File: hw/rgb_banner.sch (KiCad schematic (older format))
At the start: 8 parts, among them P1 TST, P2 TST, P3 TST, P4 TST, U1 WS2812B, U2 WS2812B, U3 WS2812B, U4 WS2812B

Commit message: schematic pretty much done, start layout
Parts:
- removed U1, U2, U3, U4: WS2812B, symbol WS2812B
- added P4: +5V, kicadlib:TEST_0.100, symbol TST
- added P5: GND, kicadlib:TEST_0.100, symbol TST
- P1: value TST -> +5V; footprint (none) -> kicadlib:TEST_0.100
- P2: value TST -> GND; footprint (none) -> kicadlib:TEST_0.100
- P3: value TST -> DIN; footprint (none) -> kicadlib:TEST_0.100
- P6: renamed from P4; value TST -> DOUT; footprint (none) -> kicadlib:TEST_0.100
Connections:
- net labels added: gnd
- net labels removed: GND
- wire segments 27 -> 19
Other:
- moved on the sheet: P1, P2, P3, P6
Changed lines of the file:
@@
 $Descr A4 11693 8268
 encoding utf-8
-Sheet 1 1
+Sheet 1 3
 Title ""
 Date ""
@@
 $EndDescr
 $Comp
-L WS2812B U1
-U 1 1 556C6577
-P 4050 2100
-F 0 "U1" H 4050 1850 60  0000 C CNN
-F 1 "WS2812B" H 4050 2300 60  0000 C CNN
-F 2 "" H 4350 1950 60  0000 C CNN
-F 3 "" H 4350 1950 60  0000 C CNN
-	1    4050 2100
-	-1   0    0    1
-$EndComp
-$Comp
-L WS2812B U2
-U 1 1 556C661E
-P 5150 2100
-F 0 "U2" H 5150 1850 60  0000 C CNN
-F 1 "WS2812B" H 5150 2300 60  0000 C CNN
-F 2 "" H 5450 1950 60  0000 C CNN
-F 3 "" H 5450 1950 60  0000 C CNN
-	1    5150 2100
-	-1   0    0    1
-$EndComp
-$Comp
-L WS2812B U3
-U 1 1 556C6646
-P 6250 2100
-F 0 "U3" H 6250 1850 60  0000 C CNN
-F 1 "WS2812B" H 6250 2300 60  0000 C CNN
-F 2 "" H 6550 1950 60  0000 C CNN
-F 3 "" H 6550 1950 60  0000 C CNN
-	1    6250 2100
-	-1   0    0    1
-$EndComp
-$Comp
-L WS2812B U4
-U 1 1 556C6673
-P 7350 2100
-F 0 "U4" H 7350 1850 60  0000 C CNN
-F 1 "WS2812B" H 7350 2300 60  0000 C CNN
-F 2 "" H 7650 1950 60  0000 C CNN
-F 3 "" H 7650 1950 60  0000 C CNN
-	1    7350 2100
-	-1   0    0    1
-$EndComp
-Text Label 3350 2500 2    60   ~ 0
-+5V
-$Comp
-L GND #PWR01
-U 1 1 556C66A2
-P 3350 1800
-F 0 "#PWR01" H 3350 1800 30  0001 C CNN
-F 1 "GND" H 3350 1730 30  0001 C CNN
-F 2 "" H 3350 1800 60  0000 C CNN
-F 3 "" H 3350 1800 60  0000 C CNN
-	1    3350 1800
-	1    0    0    -1
-$EndComp
-Wire Wire Line
-	3600 2000 3600 1700
-Wire Wire Line
-	3350 1700 5800 1700
-Wire Wire Line
-	3350 1700 3350 1800
-Text Label 3350 2150 2    60   ~ 0
-d_in
-Wire Wire Line
-	3350 2150 3600 2150
-Wire Wire Line
-	3350 2500 7800 2500
-Wire Wire Line
-	4500 2500 4500 2150
-Wire Wire Line
-	4500 2000 4600 2000
-Wire Wire Line
-	4600 2000 4600 2150
-Wire Wire Line
-	4600 2150 4700 2150
-Wire Wire Line
-	5600 2000 5700 2000
-Wire Wire Line
-	5700 2000 5700 2150
-Wire Wire Line
-	5700 2150 5800 2150
-Wire Wire Line
-	5600 2500 5600 2150
-Connection ~ 4500 2500
-Wire Wire Line
-	4700 1700 4700 2000
-Connection ~ 3600 1700
-Wire Wire Line
-	5800 1700 5800 2000
-Connection ~ 4700 1700
-Wire Wire Line
-	5850 1700 6900 1700
-Wire Wire Line
-	6900 1700 6900 2000
-Wire Wire Line
-	6700 2500 6700 2150
-Connection ~ 5600 2500
-Wire Wire Line
-	7800 2500 7800 2150
-Connection ~ 6700 2500
-Wire Wire Line
-	6700 2000 6800 2000
-Wire Wire Line
-	6800 2000 6800 2150
-Wire Wire Line
-	6800 2150 6900 2150
-Text Label 7900 2000 0    60   ~ 0
-d_out
-Wire Wire Line
-	7900 2000 7800 2000
-$Comp
 L TST P1
 U 1 1 556C686B
-P 1850 2100
-F 0 "P1" H 1850 2400 40  0000 C CNN
-F 1 "TST" H 1850 2350 30  0000 C CNN
-F 2 "" H 1850 2100 60  0000 C CNN
-F 3 "" H 1850 2100 60  0000 C CNN
-	1    1850 2100
+P 4350 3500
+F 0 "P1" H 4350 3800 40  0000 C CNN
+F 1 "+5V" H 4350 3750 30  0000 C CNN
+F 2 "kicadlib:TEST_0.100" H 4350 3500 60  0001 C CNN
+F 3 "" H 4350 3500 60  0000 C CNN
+	1    4350 3500
 	1    0    0    -1
 $EndComp
@@
 L TST P2
 U 1 1 556C69BB
-P 2000 2200
-F 0 "P2" H 2000 2500 40  0000 C CNN
-F 1 "TST" H 2000 2450 30  0000 C CNN
-F 2 "" H 2000 2200 60  0000 C CNN
-F 3 "" H 2000 2200 60  0000 C CNN
-	1    2000 2200
+P 4050 3650
+F 0 "P2" H 4050 3950 40  0000 C CNN
+F 1 "GND" H 4050 3900 30  0000 C CNN
+F 2 "kicadlib:TEST_0.100" H 4050 3650 60  0001 C CNN
+F 3 "" H 4050 3650 60  0000 C CNN
+	1    4050 3650
 	1    0    0    -1
 $EndComp
@@
 L TST P3
 U 1 1 556C69DB
-P 2150 2300
-F 0 "P3" H 2150 2600 40  0000 C CNN
-F 1 "TST" H 2150 2550 30  0000 C CNN
-F 2 "" H 2150 2300 60  0000 C CNN
-F 3 "" H 2150 2300 60  0000 C CNN
-	1    2150 2300
+P 3750 3800
+F 0 "P3" H 3750 4100 40  0000 C CNN
+F 1 "DIN" H 3750 4050 30  0000 C CNN
+F 2 "kicadlib:TEST_0.100" H 3750 3800 60  0001 C CNN
+F 3 "" H 3750 3800 60  0000 C CNN
+	1    3750 3800
 	1    0    0    -1
 $EndComp
 $Comp
-L TST P4
+L TST P6
 U 1 1 556C69FA
-P 2300 2400
-F 0 "P4" H 2300 2700 40  0000 C CNN
-F 1 "TST" H 2300 2650 30  0000 C CNN
-F 2 "" H 2300 2400 60  0000 C CNN
-F 3 "" H 2300 2400 60  0000 C CNN
-	1    2300 2400
+P 7050 3800
+F 0 "P6" H 7050 4100 40  0000 C CNN
+F 1 "DOUT" H 7050 4050 30  0000 C CNN
+F 2 "kicadlib:TEST_0.100" H 7050 3800 60  0001 C CNN
+F 3 "" H 7050 3800 60  0000 C CNN
+	1    7050 3800
 	1    0    0    -1
 $EndComp
-Text Label 1850 2200 3    60   ~ 0
+Text Label 4300 3600 2    60   ~ 0
 +5V
+Text Label 3700 3900 2    60   ~ 0
+d_in
+Text Label 7100 3900 0    60   ~ 0
+d_out
+Wire Wire Line
+	3750 3800 3750 3900
+Wire Wire Line
+	4050 3750 4050 3650
+Wire Wire Line
+	4350 3600 4350 3500
 $Comp
-L GND #PWR02
-U 1 1 556C6A24
-P 2000 2300
-F 0 "#PWR02" H 2000 2300 30  0001 C CNN
-F 1 "GND" H 2000 2230 30  0001 C CNN
-F 2 "" H 2000 2300 60  0000 C CNN
-F 3 "" H 2000 2300 60  0000 C CNN
-	1    2000 2300
+L TST P4
+U 1 1 556C71D9
+P 6450 3500
+F 0 "P4" H 6450 3800 40  0000 C CNN
+F 1 "+5V" H 6450 3750 30  0000 C CNN
+F 2 "kicadlib:TEST_0.100" H 6450 3500 60  0001 C CNN
+F 3 "" H 6450 3500 60  0000 C CNN
+	1    6450 3500
 	1    0    0    -1
 $EndComp
-Text Label 2150 2400 3    60   ~ 0
-d_in
-Text Label 2300 2500 3    60   ~ 0
-d_out
+$Comp
+L TST P5
+U 1 1 556C71DF
+P 6750 3650
+F 0 "P5" H 6750 3950 40  0000 C CNN
+F 1 "GND" H 6750 3900 30  0000 C CNN
+F 2 "kicadlib:TEST_0.100" H 6750 3650 60  0001 C CNN
+F 3 "" H 6750 3650 60  0000 C CNN
+	1    6750 3650
+	1    0    0    -1
+$EndComp
+Text Label 6500 3600 0    60   ~ 0
++5V
 Wire Wire Line
-	2300 2500 2300 2400
+	6450 3600 6450 3500
+Text Label 4000 3750 2    60   ~ 0
+gnd
+$Sheet
+S 5600 3500 750  1600
+U 556C8A1A
+F0 "digit2" 60
+F1 "digit2.sch" 60
+F2 "gnd" I R 6350 3750 60
+F3 "+5V" I R 6350 3600 60
+F4 "d_in_1" I L 5600 4050 60
+F5 "d_out_all" I R 6350 3900 60
+F6 "d_in_2" I L 5600 4350 60
+F7 "d_in_3" I L 5600 4650 60
+F8 "d_out_1" I L 5600 4200 60
+F9 "d_out_2" I L 5600 4500 60
+F10 "d_out_3" I L 5600 4800 60
+F11 "d_in_4" I L 5600 4950 60
+$EndSheet
 Wire Wire Line
-	2150 2300 2150 2400
+	3700 3900 4450 3900
 Wire Wire Line
-	2000 2300 2000 2200
+	4000 3750 4450 3750
 Wire Wire Line
-	1850 2200 1850 2100
+	4300 3600 4450 3600
+Connection ~ 4350 3600
+Connection ~ 4050 3750
+Connection ~ 3750 3900
+Text Label 6800 3750 0    60   ~ 0
+gnd
+Wire Wire Line
+	6350 3600 6500 3600
+Connection ~ 6450 3600
+Wire Wire Line
+	6350 3750 6800 3750
+Wire Wire Line
+	6750 3750 6750 3650
+Wire Wire Line
+	6350 3900 7100 3900
+Wire Wire Line
+	7050 3900 7050 3800
+Connection ~ 6750 3750
+Connection ~ 7050 3900
+$Sheet
+S 4450 3500 750  1600
+U 556C8146
+F0 "digit1" 60
+F1 "digit1.sch" 60
+F2 "gnd" I L 4450 3750 60
+F3 "+5V" I L 4450 3600 60
+F4 "d_in_all" I L 4450 3900 60
+F5 "d_out_3" I R 5200 4650 60
+F6 "d_out_4" I R 5200 4950 60
+F7 "d_in_3" I R 5200 4800 60
+F8 "d_in_2" I R 5200 4500 60
+F9 "d_out_2" I R 5200 4350 60
+F10 "d_in_1" I R 5200 4200 60
+F11 "d_out_1" I R 5200 4050 60
+$EndSheet
+Wire Wire Line
+	5200 4050 5600 4050
+Wire Wire Line
+	5600 4200 5200 4200
+Wire Wire Line
+	5200 4350 5600 4350
+Wire Wire Line
+	5600 4500 5200 4500
+Wire Wire Line
+	5200 4650 5600 4650
+Wire Wire Line
+	5600 4800 5200 4800
+Wire Wire Line
+	5200 4950 5600 4950
 $EndSCHEMATC

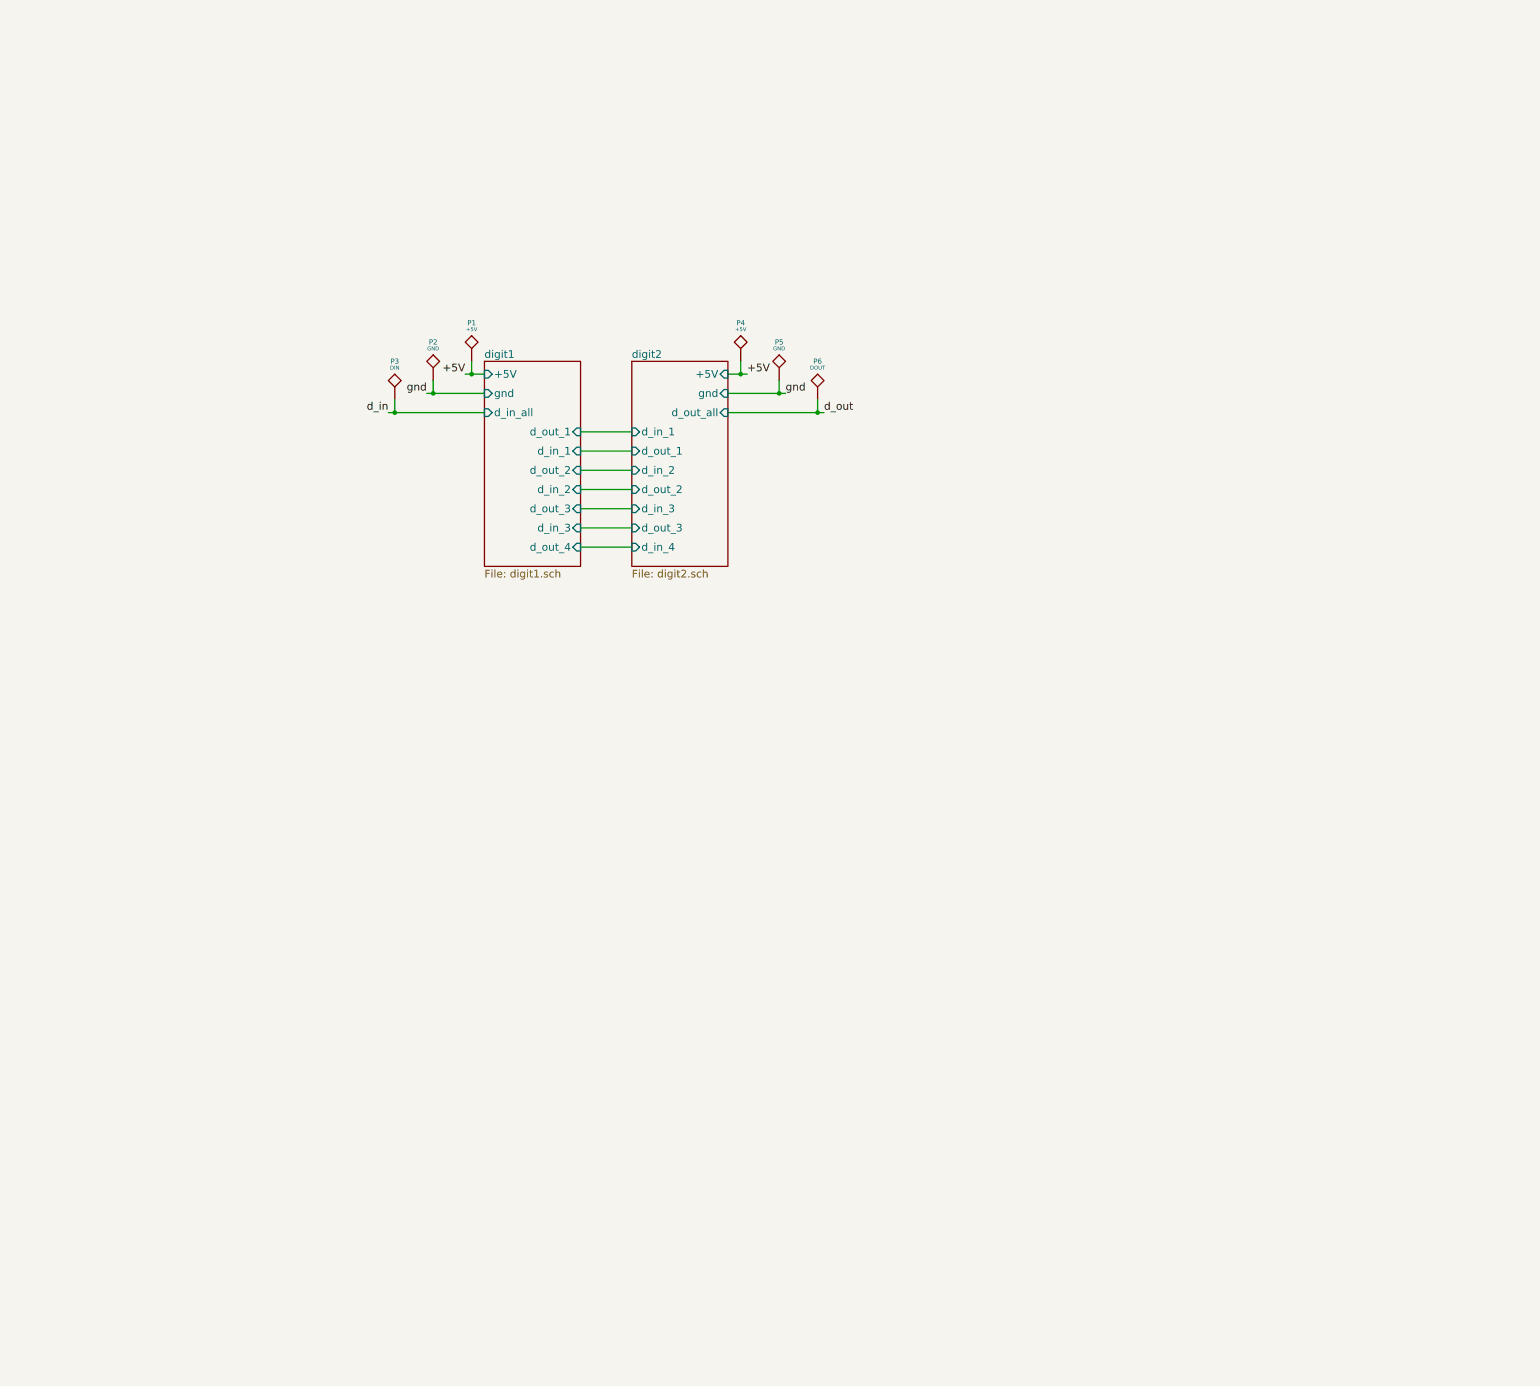
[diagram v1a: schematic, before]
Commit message: start consolidating schematic
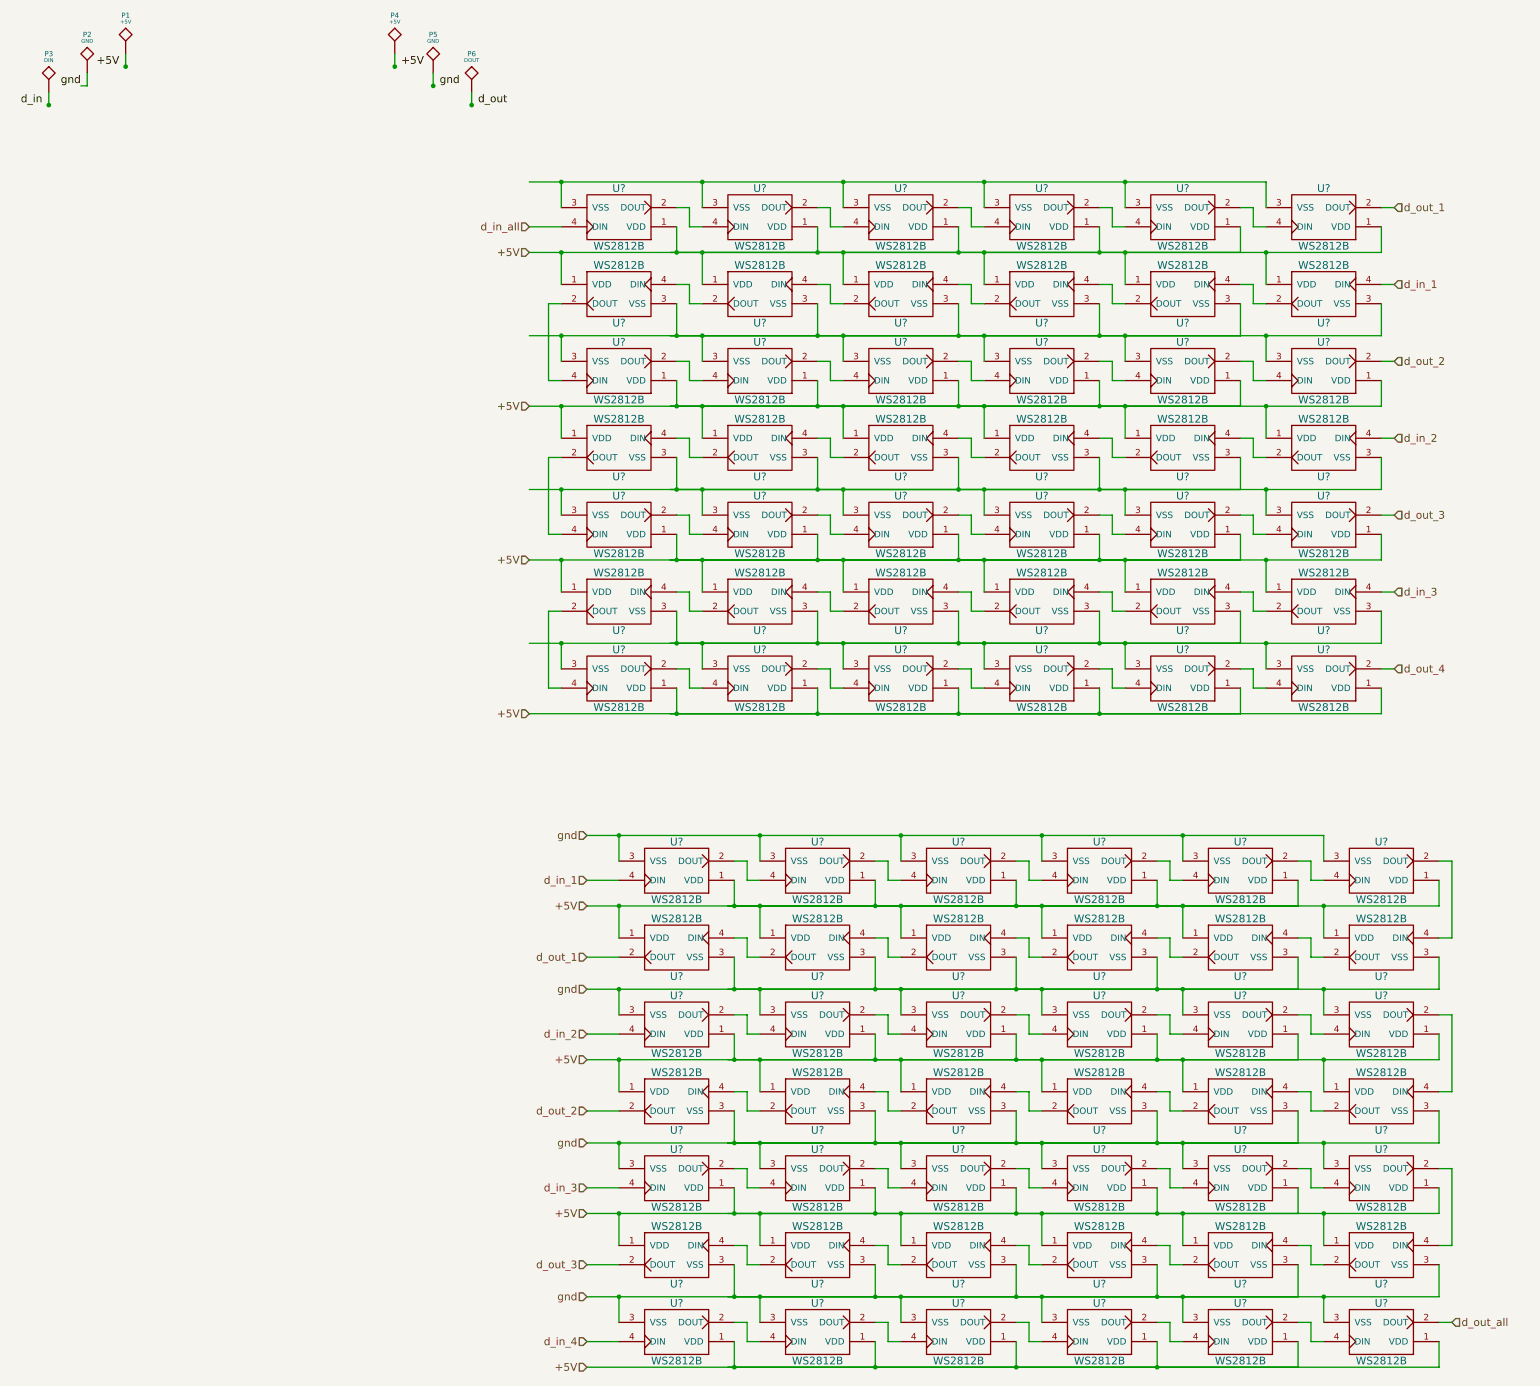
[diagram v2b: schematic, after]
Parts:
- added U? (x84): WS2812B, kicadlib:WS2812B_SMD_5050, symbol WS2812B
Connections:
- net labels added: d_in_1, d_in_2, d_in_3, d_in_4, d_in_all, d_out_1, d_out_2, d_out_3, d_out_4, d_out_all
- wire segments 19 -> 449
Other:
- moved on the sheet: P1, P2, P3, P4, P5, P6

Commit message: pcb layout. zones not working.
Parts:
- gave numbers to parts that had none: 84
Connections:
- net labels removed: d_in_1, d_in_2, d_in_3, d_in_4, d_in_all, d_out_1, d_out_2, d_out_3, d_out_4, d_out_all
- wire segments 449 -> 446
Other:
- moved on the sheet: P1, P2, P3, P4, P5, P6, U1, U10, U11, U12, U13, U14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

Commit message: work on pcb
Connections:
- net +5V: now also U11.1 (VDD), U35.1 (VDD), U59.1 (VDD), U83.1 (VDD)
- net gnd: now also U23.3 (VSS), U47.3 (VSS), U71.3 (VSS)
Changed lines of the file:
@@
 LIBS:memory
 LIBS:xilinx
-LIBS:special
 LIBS:microcontrollers
 LIBS:dsp
@@
 Connection ~ 7800 5800
 Wire Wire Line
-	7800 6000 7800 5800
+	7800 5800 7800 6000
 Wire Wire Line
 	7700 6150 7800 6150
@@
 Wire Wire Line
 	7600 6000 7700 6000
-Wire Wire Line
-	3150 5800 15300 5800
 Wire Wire Line
 	8700 6350 8700 6150
@@
 	3400 5800 3400 6000
 Wire Wire Line
-	2050 5800 7600 5800
+	2050 5800 15300 5800
 Wire Wire Line
 	2300 6000 2300 5800
@@
 	8900 5800 8900 6000
 Connection ~ 13100 6350
-Wire Wire Line
-	14200 6350 14200 6150
 Connection ~ 12000 6350
 Wire Wire Line
@@
 	8900 4600 8900 4800
 Connection ~ 13100 5150
-Wire Wire Line
-	14200 5150 14200 4950
 Connection ~ 12000 5150
 Wire Wire Line
@@
 	13300 3950 13300 4200
 Connection ~ 13100 4600
-Wire Wire Line
-	14200 4600 14200 4350
 Connection ~ 12000 4600
 Wire Wire Line
@@
 	8900 3400 8900 3600
 Connection ~ 13100 3950
-Wire Wire Line
-	14200 3950 14200 3750
 Connection ~ 12000 3950
 Wire Wire Line
@@
 	13300 2750 13300 3000
 Connection ~ 13100 3400
-Wire Wire Line
-	14200 3400 14200 3150
 Connection ~ 12000 3400
 Wire Wire Line
@@
 	8900 2200 8900 2400
 Connection ~ 13100 2750
-Wire Wire Line
-	14200 2750 14200 2550
 Connection ~ 12000 2750
 Wire Wire Line
@@
 Text Label 2050 5800 2    60   ~ 0
 gnd
+Connection ~ 7600 5800
+Connection ~ 14200 5800
+Wire Wire Line
+	14200 5150 14200 4950
+Connection ~ 14200 5150
+Wire Wire Line
+	14200 6150 14200 6350
+Connection ~ 14200 6350
+Wire Wire Line
+	14200 4350 14200 4600
+Connection ~ 14200 4600
+Wire Wire Line
+	14200 3950 14200 3750
+Connection ~ 14200 3950
+Wire Wire Line
+	14200 3400 14200 3150
+Connection ~ 14200 3400
+Wire Wire Line
+	14200 2750 14200 2550
+Connection ~ 14200 2750
 $EndSCHEMATC
